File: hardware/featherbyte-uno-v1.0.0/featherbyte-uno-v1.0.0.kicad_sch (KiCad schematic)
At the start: 60 parts, among them J1 Conn_01x08, J10 Conn_01x09, J2 Conn_01x10, J3 Conn_01x06, J5 USB_C_Receptacle_16P, J6 SWD Connector, J7 Terminal Block, J8 USB_C_Receptacle_16P, J9 BOOT1, SW1 Reset, SW2 BOOT0, SW3 SW_DIP_x04, U1 CH32V203CxT6, U2 TJA1050, U4 AMS1117-3.3, U5 USBLC6-2P6, U6 USBLC6-2P6, Y1 8M, Y3 32.768K

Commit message: routing process ongoing
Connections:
- net D2: now also U1.16 (PA6/ADC6)
- net D3: now also U1.17 (PA7/ADC7)
- net D4: now also U1.29 (PA8)
- net D5: now also U1.30 (PA9)
- net D6: now also U1.31 (PA10)
- net D7: now also U1.38 (PA15)
- net D8: now also U1.39 (PB3)
- net D9: now also U1.40 (PB4)
- net LED: now also U1.41 (PB5)
- net VREF: no longer J2.3 (Pin_3)
- no-connect marks 7 -> 8
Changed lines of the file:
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@@
 	)
 	(no_connect
+		(at 69.85 173.99)
+	)
+	(no_connect
 		(at 125.73 57.15)
 	)
@@
 	(wire
 		(pts
+			(xy 248.92 128.27) (xy 245.11 128.27)
+		)
+		(stroke
+			(width 0)
+			(type default)
+		)
+	)
+	(wire
+		(pts
 			(xy 271.78 38.1) (xy 259.08 38.1)
 		)
@@
 	(wire
 		(pts
-			(xy 74.93 173.99) (xy 69.85 173.99)
-		)
-		(stroke
-			(width 0)
-			(type default)
-		)
-	)
-	(wire
-		(pts
 			(xy 114.3 171.45) (xy 111.76 171.45)
 		)
@@
 	(wire
 		(pts
+			(xy 200.66 119.38) (xy 204.47 119.38)
+		)
+		(stroke
+			(width 0)
+			(type default)
+		)
+	)
+	(wire
+		(pts
 			(xy 222.25 73.66) (xy 222.25 76.2)
 		)
@@
 	(wire
 		(pts
+			(xy 248.92 135.89) (xy 245.11 135.89)
+		)
+		(stroke
+			(width 0)
+			(type default)
+		)
+	)
+	(wire
+		(pts
 			(xy 110.49 167.64) (xy 111.76 167.64)
 		)
@@
 	(wire
 		(pts
+			(xy 200.66 114.3) (xy 204.47 114.3)
+		)
+		(stroke
+			(width 0)
+			(type default)
+		)
+	)
+	(wire
+		(pts
 			(xy 82.55 113.03) (xy 82.55 114.3)
 		)
@@
 	(wire
 		(pts
+			(xy 248.92 125.73) (xy 245.11 125.73)
+		)
+		(stroke
+			(width 0)
+			(type default)
+		)
+	)
+	(wire
+		(pts
 			(xy 30.48 186.69) (xy 26.67 186.69)
 		)
@@
 	(wire
 		(pts
+			(xy 248.92 133.35) (xy 245.11 133.35)
+		)
+		(stroke
+			(width 0)
+			(type default)
+		)
+	)
+	(wire
+		(pts
 			(xy 26.67 165.1) (xy 34.29 165.1)
 		)
@@
 	(wire
 		(pts
+			(xy 248.92 151.13) (xy 245.11 151.13)
+		)
+		(stroke
+			(width 0)
+			(type default)
+		)
+	)
+	(wire
+		(pts
 			(xy 162.56 123.19) (xy 151.13 123.19)
 		)
@@
 	(wire
 		(pts
+			(xy 248.92 130.81) (xy 245.11 130.81)
+		)
+		(stroke
+			(width 0)
+			(type default)
+		)
+	)
+	(wire
+		(pts
 			(xy 74.93 186.69) (xy 69.85 186.69)
 		)
@@
 	(wire
 		(pts
+			(xy 200.66 116.84) (xy 204.47 116.84)
+		)
+		(stroke
+			(width 0)
+			(type default)
+		)
+	)
+	(wire
+		(pts
 			(xy 248.92 110.49) (xy 245.11 110.49)
 		)
@@
 	)
 	(label "D2"
-		(at 261.62 129.54 180)
+		(at 248.92 125.73 180)
 		(effects
 			(font
@@
 	)
 	(label "D9"
-		(at 193.04 152.4 0)
+		(at 200.66 116.84 0)
 		(effects
 			(font
@@
 		)
 	)
-	(label "VREF"
-		(at 74.93 173.99 180)
-		(effects
-			(font
-				(size 1.27 1.27)
-			)
-			(justify right bottom)
-		)
-	)
 	(label "D2"
 		(at 53.34 186.69 180)
@@
 	)
 	(label "LED"
-		(at 209.55 163.83 0)
+		(at 200.66 119.38 0)
 		(effects
 			(font
@@
 	)
 	(label "D4"
-		(at 255.27 119.38 180)
+		(at 248.92 130.81 180)
 		(effects
 			(font
@@
 	)
 	(label "D8"
-		(at 191.77 148.59 0)
+		(at 200.66 114.3 0)
 		(effects
 			(font
@@
 	)
 	(label "D3"
-		(at 261.62 132.08 180)
+		(at 248.92 128.27 180)
 		(effects
 			(font
@@
 	)
 	(label "D5"
-		(at 255.27 121.92 180)
+		(at 248.92 133.35 180)
 		(effects
 			(font
@@
 	)
 	(label "D7"
-		(at 193.04 146.05 0)
+		(at 248.92 151.13 180)
 		(effects
 			(font
 				(size 1.27 1.27)
 			)
-			(justify left bottom)
+			(justify right bottom)
 		)
 	)
@@
 	)
 	(label "D6"
-		(at 255.27 124.46 180)
+		(at 248.92 135.89 180)
 		(effects
 			(font

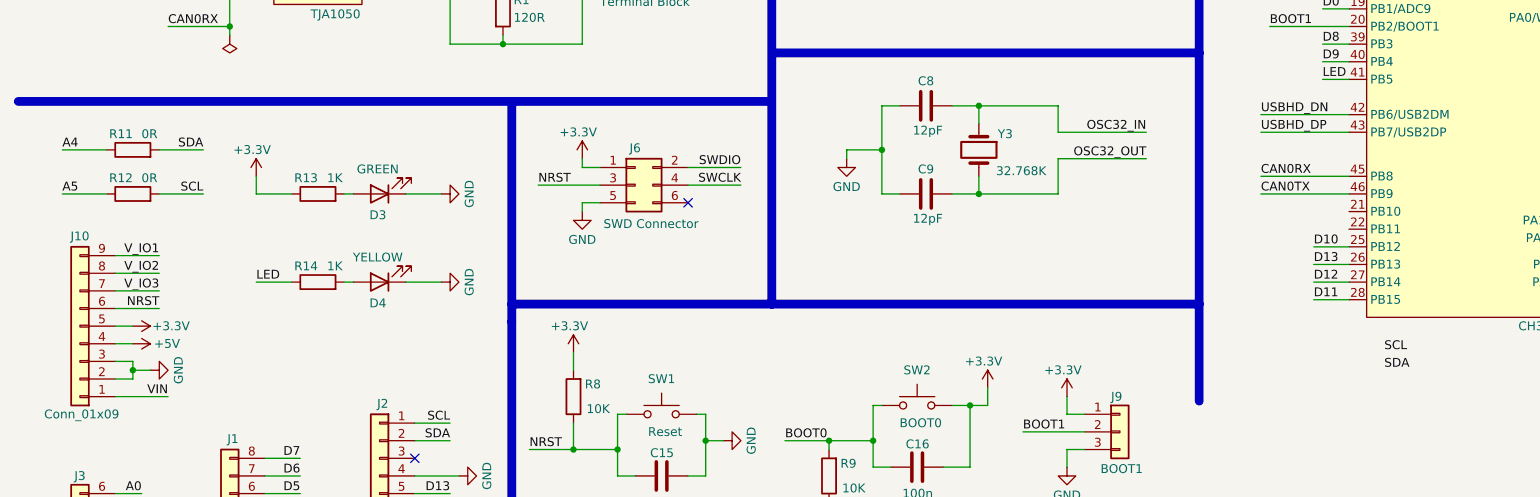
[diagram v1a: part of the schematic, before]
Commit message: all pins routed
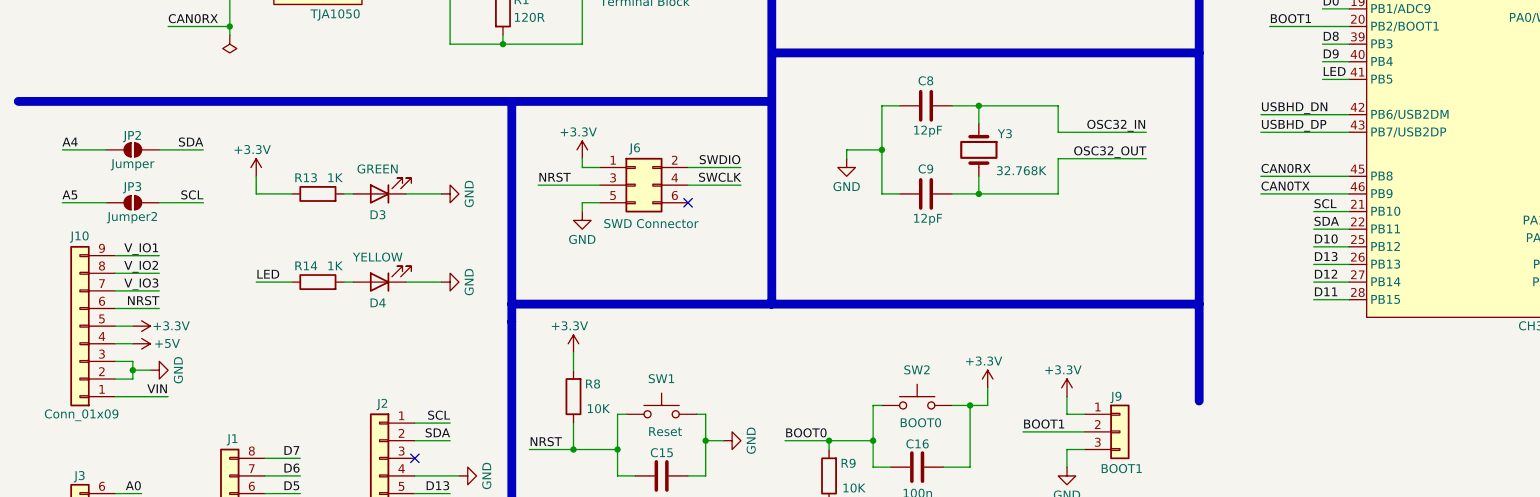
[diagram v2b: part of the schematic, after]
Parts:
- removed R11, R12: 0R, Resistor_SMD:R_0603_1608Metric, symbol Device:R
- added JP2: Jumper, Jumper:SolderJumper-2_P1.3mm_Open_TrianglePad1.0x1.5mm, symbol Jumper:SolderJumper_2_Open
- added JP3: Jumper2, Jumper:SolderJumper-2_P1.3mm_Open_TrianglePad1.0x1.5mm, symbol Jumper:SolderJumper_2_Open
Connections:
- net A4: now also JP2.1 (A)
- net A5: now also JP3.1 (A)
- net SCL: now also U1.21 (PB10), JP3.2 (B)
- net SDA: now also U1.22 (PB11), JP2.2 (B)
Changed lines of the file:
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@@
 	(wire
 		(pts
-			(xy 39.37 135.89) (xy 33.02 135.89)
+			(xy 39.37 137.16) (xy 33.02 137.16)
 		)
 		(stroke
@@
 	(wire
 		(pts
+			(xy 199.39 140.97) (xy 204.47 140.97)
+		)
+		(stroke
+			(width 0)
+			(type default)
+		)
+	)
+	(wire
+		(pts
 			(xy 153.67 36.83) (xy 154.94 36.83)
 		)
@@
 	(wire
 		(pts
+			(xy 199.39 138.43) (xy 204.47 138.43)
+		)
+		(stroke
+			(width 0)
+			(type default)
+		)
+	)
+	(wire
+		(pts
 			(xy 93.98 132.08) (xy 96.52 132.08)
 		)
@@
 	(wire
 		(pts
-			(xy 19.05 135.89) (xy 25.4 135.89)
+			(xy 19.05 137.16) (xy 25.4 137.16)
 		)
 		(stroke
@@
 	)
 	(label "SCL"
-		(at 209.55 158.75 0)
+		(at 199.39 138.43 0)
 		(effects
 			(font
@@
 	)
 	(label "SCL"
-		(at 39.37 135.89 180)
+		(at 39.37 137.16 180)
 		(effects
 			(font
@@
 	)
 	(label "SDA"
-		(at 209.55 161.29 0)
+		(at 199.39 140.97 0)
 		(effects
 			(font
@@
 	)
 	(label "A5"
-		(at 19.05 135.89 0)
+		(at 19.05 137.16 0)
 		(effects
 			(font
@@
 	)
 	(symbol
+		(lib_id "Jumper:SolderJumper_2_Open")
+		(at 29.21 129.54 0)
+		(unit 1)
+		(exclude_from_sim no)
+		(in_bom no)
+		(on_board yes)
+		(dnp no)
+		(property "Reference" "JP2"
+			(at 29.21 127.508 0)
+			(effects
+				(font
+					(size 1.27 1.27)
+				)
+			)
+		)
+		(property "Value" "Jumper"
+			(at 29.21 131.572 0)
+			(effects
+				(font
+					(size 1.27 1.27)
+				)
+			)
+		)
+		(property "Footprint" "Jumper:SolderJumper-2_P1.3mm_Open_TrianglePad1.0x1.5mm"
+			(at 29.21 129.54 0)
+			(effects
+				(font
+					(size 1.27 1.27)
+				)
+				(hide yes)
+			)
+		)
+		(property "Datasheet" "~"
+			(at 29.21 129.54 0)
+			(effects
+				(font
+					(size 1.27 1.27)
+				)
+				(hide yes)
+			)
+		)
+		(property "Description" "Solder Jumper, 2-pole, open"
+			(at 29.21 129.54 0)
+			(effects
+				(font
+					(size 1.27 1.27)
+				)
+				(hide yes)
+			)
+		)
+		(pin "2"
+		)
+		(pin "1"
+		)
+		(instances
+			(project "featherbyte-uno-v1.0.0"
+				(path "/9057772d-fe42-4f07-905a-9d3ca3415356"
+					(reference "JP2")
+					(unit 1)
+				)
+			)
+		)
+	)
+	(symbol
 		(lib_id "power:VBUS")
 		(at 69.85 45.72 0)
@@
 	)
 	(symbol
-		(lib_id "Device:R")
-		(at 29.21 129.54 90)
-		(unit 1)
-		(exclude_from_sim no)
-		(in_bom yes)
-		(on_board yes)
-		(dnp no)
-		(property "Reference" "R11"
-			(at 29.21 127.254 90)
-			(effects
-				(font
-					(size 1.27 1.27)
-				)
-				(justify left)
-			)
-		)
-		(property "Value" "0R"
-			(at 32.766 127.254 90)
-			(effects
-				(font
-					(size 1.27 1.27)
-				)
-				(justify left)
-			)
-		)
-		(property "Footprint" "Resistor_SMD:R_0603_1608Metric"
-			(at 29.21 131.318 90)
-			(effects
-				(font
-					(size 1.27 1.27)
-				)
-				(hide yes)
-			)
-		)
-		(property "Datasheet" "~"
-			(at 29.21 129.54 0)
-			(effects
-				(font
-					(size 1.27 1.27)
-				)
-				(hide yes)
-			)
-		)
-		(property "Description" "Resistor"
-			(at 29.21 129.54 0)
-			(effects
-				(font
-					(size 1.27 1.27)
-				)
-				(hide yes)
-			)
-		)
-		(pin "1"
-		)
-		(pin "2"
-		)
-		(instances
-			(project "featherbyte-uno-v1.0.0"
-				(path "/9057772d-fe42-4f07-905a-9d3ca3415356"
-					(reference "R11")
-					(unit 1)
-				)
-			)
-		)
-	)
-	(symbol
 		(lib_id "power:PWR_FLAG")
 		(at 43.18 113.03 180)
@@
 	)
 	(symbol
+		(lib_id "Jumper:SolderJumper_2_Open")
+		(at 29.21 137.16 0)
+		(unit 1)
+		(exclude_from_sim no)
+		(in_bom no)
+		(on_board yes)
+		(dnp no)
+		(property "Reference" "JP3"
+			(at 29.21 134.874 0)
+			(effects
+				(font
+					(size 1.27 1.27)
+				)
+			)
+		)
+		(property "Value" "Jumper2"
+			(at 29.21 139.192 0)
+			(effects
+				(font
+					(size 1.27 1.27)
+				)
+			)
+		)
+		(property "Footprint" "Jumper:SolderJumper-2_P1.3mm_Open_TrianglePad1.0x1.5mm"
+			(at 29.21 137.16 0)
+			(effects
+				(font
+					(size 1.27 1.27)
+				)
+				(hide yes)
+			)
+		)
+		(property "Datasheet" "~"
+			(at 29.21 137.16 0)
+			(effects
+				(font
+					(size 1.27 1.27)
+				)
+				(hide yes)
+			)
+		)
+		(property "Description" "Solder Jumper, 2-pole, open"
+			(at 29.21 137.16 0)
+			(effects
+				(font
+					(size 1.27 1.27)
+				)
+				(hide yes)
+			)
+		)
+		(pin "2"
+		)
+		(pin "1"
+		)
+		(instances
+			(project "featherbyte-uno-v1.0.0"
+				(path "/9057772d-fe42-4f07-905a-9d3ca3415356"
+					(reference "JP3")
+					(unit 1)
+				)
+			)
+		)
+	)
+	(symbol
 		(lib_id "Device:R")
 		(at 55.88 135.89 90)
@@
 					(unit 1)
 				)
-			)
-		)
-	)
-	(symbol
-		(lib_id "Device:R")
-		(at 29.21 135.89 90)
-		(unit 1)
-		(exclude_from_sim no)
-		(in_bom yes)
-		(on_board yes)
-		(dnp no)
-		(property "Reference" "R12"
-			(at 29.21 133.604 90)
-			(effects
-				(font
-					(size 1.27 1.27)
-				)
-				(justify left)
-			)
-		)
-		(property "Value" "0R"
-			(at 32.766 133.604 90)
-			(effects
-				(font
-					(size 1.27 1.27)
-				)
-				(justify left)
-			)
-		)
-		(property "Footprint" "Resistor_SMD:R_0603_1608Metric"
-			(at 29.21 137.668 90)
-			(effects
-				(font
-					(size 1.27 1.27)
-				)
-				(hide yes)
-			)
-		)
-		(property "Datasheet" "~"
-			(at 29.21 135.89 0)
-			(effects
-				(font
-					(size 1.27 1.27)
-				)
-				(hide yes)
-			)
-		)
-		(property "Description" "Resistor"
-			(at 29.21 135.89 0)
-			(effects
-				(font
-					(size 1.27 1.27)
-				)
-				(hide yes)
-			)
-		)
-		(pin "1"
-		)
-		(pin "2"
-		)
-		(instances
-			(project "featherbyte-uno-v1.0.0"
-				(path "/9057772d-fe42-4f07-905a-9d3ca3415356"
-					(reference "R12")
-					(unit 1)
-				)

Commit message: all routing done
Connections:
- net GND: now also J6.6 (Pin_6)
- no-connect marks 8 -> 7
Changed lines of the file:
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@@
 		(color 0 0 0 0)
 	)
+	(junction
+		(at 102.87 143.51)
+		(diameter 0)
+		(color 0 0 0 0)
+	)
 	(no_connect
 		(at 49.53 55.88)
@@
 		(at 49.53 58.42)
 	)
-	(no_connect
-		(at 109.22 137.16)
-	)
 	(wire
 		(pts
@@
 	(wire
 		(pts
+			(xy 111.76 143.51) (xy 102.87 143.51)
+		)
+		(stroke
+			(width 0)
+			(type default)
+		)
+	)
+	(wire
+		(pts
 			(xy 139.7 58.42) (xy 142.24 58.42)
 		)
@@
 	(wire
 		(pts
+			(xy 111.76 137.16) (xy 111.76 143.51)
+		)
+		(stroke
+			(width 0)
+			(type default)
+		)
+	)
+	(wire
+		(pts
 			(xy 137.16 45.72) (xy 137.16 60.96)
 		)
@@
 	(wire
 		(pts
+			(xy 109.22 137.16) (xy 111.76 137.16)
+		)
+		(stroke
+			(width 0)
+			(type default)
+		)
+	)
+	(wire
+		(pts
 			(xy 116.84 132.08) (xy 109.22 132.08)
 		)
@@
 	(wire
 		(pts
+			(xy 93.98 143.51) (xy 102.87 143.51)
+		)
+		(stroke
+			(width 0)
+			(type default)
+		)
+	)
+	(wire
+		(pts
 			(xy 200.66 25.4) (xy 207.01 25.4)
 		)
@@
 	(wire
 		(pts
+			(xy 102.87 144.78) (xy 102.87 143.51)
+		)
+		(stroke
+			(width 0)
+			(type default)
+		)
+	)
+	(wire
+		(pts
 			(xy 53.34 38.1) (xy 53.34 35.56)
 		)
@@
 	(wire
 		(pts
-			(xy 93.98 137.16) (xy 93.98 138.43)
+			(xy 93.98 137.16) (xy 93.98 143.51)
 		)
 		(stroke
@@
 	(symbol
 		(lib_id "power:GND")
-		(at 93.98 138.43 0)
+		(at 102.87 144.78 0)
 		(unit 1)
 		(exclude_from_sim no)
@@
 		(dnp no)
 		(property "Reference" "#PWR025"
-			(at 93.98 144.78 0)
+			(at 102.87 151.13 0)
 			(effects
 				(font
@@
 		)
 		(property "Value" "GND"
-			(at 93.98 142.494 0)
+			(at 102.87 148.336 0)
 			(effects
 				(font
@@
 		)
 		(property "Footprint" ""
-			(at 93.98 138.43 0)
+			(at 102.87 144.78 0)
 			(effects
 				(font
@@
 		)
 		(property "Datasheet" ""
-			(at 93.98 138.43 0)
+			(at 102.87 144.78 0)
 			(effects
 				(font
@@
 		)
 		(property "Description" "Power symbol creates a global label with name \"GND\" , ground"
-			(at 93.98 138.43 0)
+			(at 102.87 144.78 0)
 			(effects
 				(font
@@
 		)
 		(property "Value" "SWD Connector"
-			(at 103.886 140.208 0)
+			(at 103.632 139.7 0)
 			(effects
 				(font

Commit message: drc check process ongoing
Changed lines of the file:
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@@
 	)
 	(junction
-		(at 207.01 25.4)
-		(diameter 0)
-		(color 0 0 0 0)
-	)
-	(junction
 		(at 151.13 102.87)
 		(diameter 0)
@@
 	(wire
 		(pts
-			(xy 207.01 22.86) (xy 207.01 25.4)
+			(xy 200.66 22.86) (xy 200.66 25.4)
 		)
 		(stroke
@@
 	(wire
 		(pts
-			(xy 261.62 81.28) (xy 270.51 81.28)
-		)
-		(stroke
-			(width 0)
-			(type default)
-		)
-	)
-	(wire
-		(pts
 			(xy 248.92 120.65) (xy 245.11 120.65)
 		)
@@
 	(wire
 		(pts
-			(xy 200.66 25.4) (xy 207.01 25.4)
-		)
-		(stroke
-			(width 0)
-			(type default)
-		)
-	)
-	(wire
-		(pts
 			(xy 152.4 58.42) (xy 156.21 58.42)
 		)
@@
 	(wire
 		(pts
-			(xy 207.01 25.4) (xy 212.09 25.4)
-		)
-		(stroke
-			(width 0)
-			(type default)
-		)
-	)
-	(wire
-		(pts
 			(xy 129.54 30.48) (xy 137.16 30.48)
 		)
@@
 	(wire
 		(pts
+			(xy 200.66 25.4) (xy 212.09 25.4)
+		)
+		(stroke
+			(width 0)
+			(type default)
+		)
+	)
+	(wire
+		(pts
 			(xy 154.94 36.83) (xy 154.94 44.45)
 		)
@@
 	(wire
 		(pts
+			(xy 261.62 81.28) (xy 270.51 81.28)
+		)
+		(stroke
+			(width 0)
+			(type default)
+		)
+	)
+	(wire
+		(pts
 			(xy 26.67 152.4) (xy 33.02 152.4)
 		)
@@
 	)
 	(label "VIN"
-		(at 201.93 25.4 0)
+		(at 204.47 25.4 0)
 		(effects
 			(font
@@
 	(symbol
 		(lib_id "power:PWR_FLAG")
-		(at 207.01 22.86 0)
+		(at 200.66 22.86 0)
 		(unit 1)
 		(exclude_from_sim no)
@@
 		(dnp no)
 		(property "Reference" "#FLG03"
-			(at 207.01 20.955 0)
+			(at 200.66 20.955 0)
 			(effects
 				(font
@@
 		)
 		(property "Value" "PWR_FLAG"
-			(at 207.264 19.05 0)
+			(at 200.914 19.05 0)
 			(effects
 				(font
@@
 		)
 		(property "Footprint" ""
-			(at 207.01 22.86 0)
+			(at 200.66 22.86 0)
 			(effects
 				(font
@@
 		)
 		(property "Datasheet" "~"
-			(at 207.01 22.86 0)
+			(at 200.66 22.86 0)
 			(effects
 				(font
@@
 		)
 		(property "Description" "Special symbol for telling ERC where power comes from"
-			(at 207.01 22.86 0)
+			(at 200.66 22.86 0)
 			(effects
 				(font

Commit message: pin labeling and drc checks has been done
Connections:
- net GND: now also J2.3 (Pin_3)
- no-connect marks 7 -> 6
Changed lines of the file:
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@@
+		(color 0 0 0 0)
+	)
+	(junction
+		(at 72.39 176.53)
+		(diameter 0)
 		(color 0 0 0 0)
 	)
@@
 	)
 	(no_connect
-		(at 69.85 173.99)
-	)
-	(no_connect
 		(at 125.73 57.15)
 	)
@@
 	(wire
 		(pts
-			(xy 69.85 176.53) (xy 76.2 176.53)
+			(xy 69.85 176.53) (xy 72.39 176.53)
 		)
 		(stroke
@@
 	(wire
 		(pts
+			(xy 72.39 176.53) (xy 76.2 176.53)
+		)
+		(stroke
+			(width 0)
+			(type default)
+		)
+	)
+	(wire
+		(pts
 			(xy 157.48 170.18) (xy 166.37 170.18)
 		)
@@
 	(wire
 		(pts
+			(xy 69.85 173.99) (xy 72.39 173.99)
+		)
+		(stroke
+			(width 0)
+			(type default)
+		)
+	)
+	(wire
+		(pts
 			(xy 82.55 104.14) (xy 82.55 105.41)
 		)
@@
 		)
 		(stroke
+			(width 0)
+			(type default)
+		)
+	)
+	(wire
+		(pts
+			(xy 72.39 173.99) (xy 72.39 176.53)
+		)
+		(stroke

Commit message: version info addition and adc pin correction done
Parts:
- JP1, JP2, JP3: now in the parts list

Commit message: schematics updated for visual reasons
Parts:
- J6: value SWD Connector -> Conn_02x03
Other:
- note added: "Arduino UNO Compatible Headers"
- note added: "BOOT1 Jumper"
- note added: "CAN Transreceiver"
- note added: "CH32V203 Microcontroller Unit"
- note added: "Device/Host mode selection via CC pins"
- note added: "High Frequency Oscillator"
- note added: "Juper for connecting SCL and SDA pin to A5 and A4 pins"
- note added: "Linear Regulator & Iput protection"
- note added: "Low Frequency Oscillator"
- note added: "Power LED"
- note added: "Reset and Boot Buttons"
- note added: "SWD Programing Connector"
- note added: "Termination resistance selection"
- note added: "USB-C Device Only & Power Input"
- note added: "USB-C Host + Device Only & Power Input"
- note added: "User LED"
- title: featherbyte-uno Root -> featherbyte-uno
- moved on the sheet: C1, C10, C11, C12, C13, C14, C15, C16, C17, C2, C3, C4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

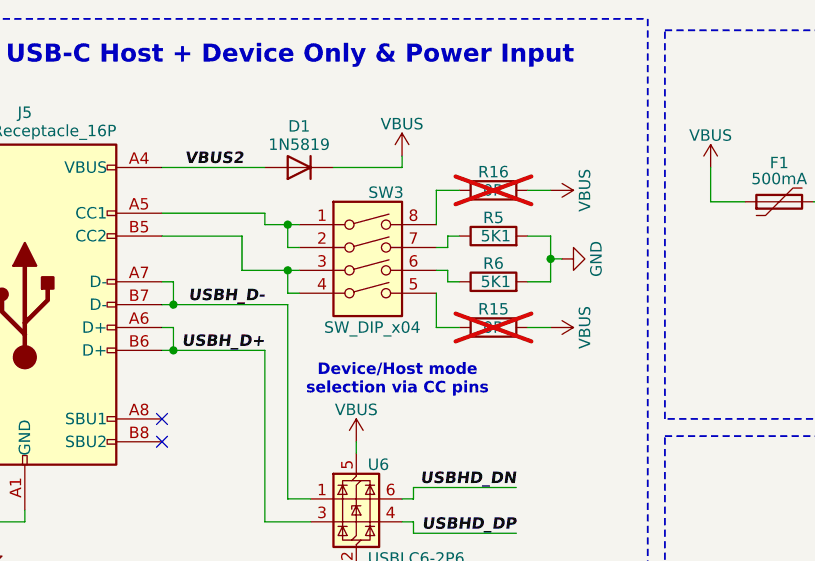
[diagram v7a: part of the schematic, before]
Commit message: actual mcu pin names added to back silk screen layer
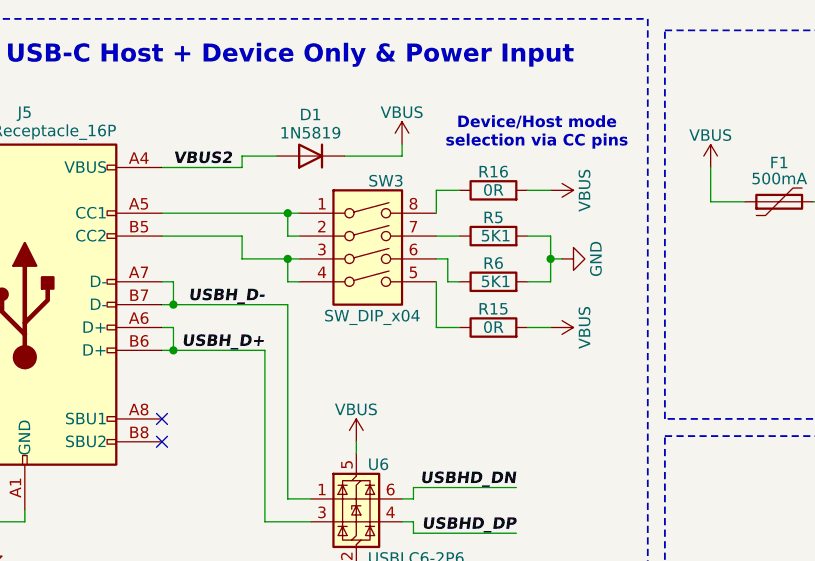
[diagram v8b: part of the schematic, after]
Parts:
- R15, R16: now fitted
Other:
- moved on the sheet: D1, SW3
